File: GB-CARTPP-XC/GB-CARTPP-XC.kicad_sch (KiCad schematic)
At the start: 29 parts

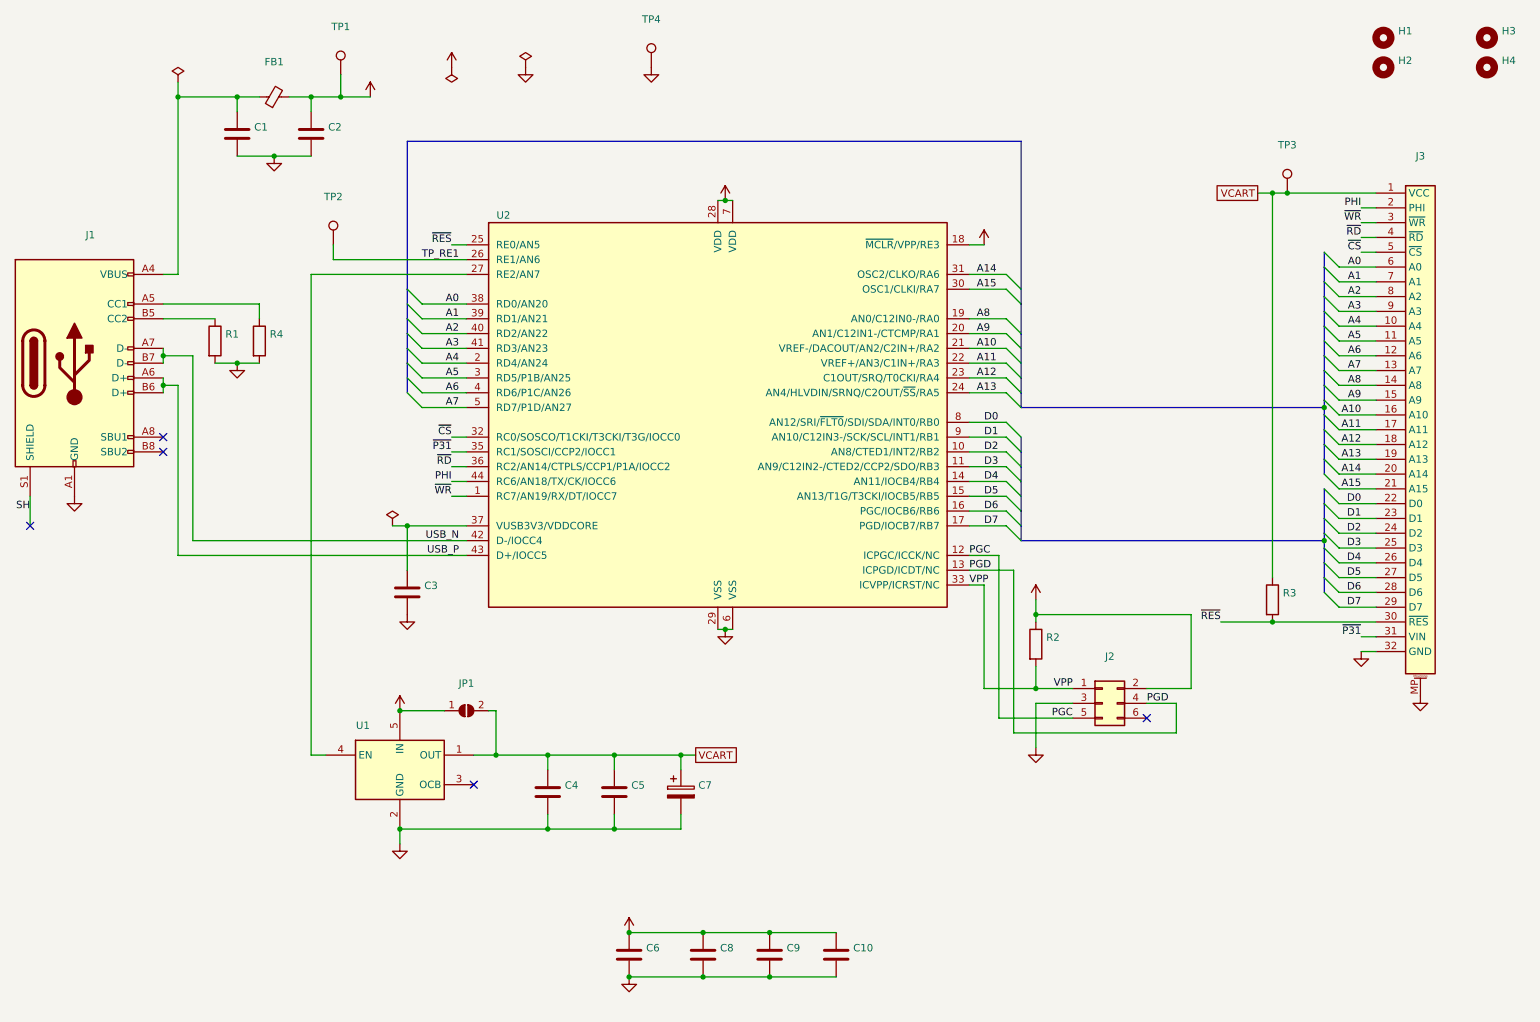
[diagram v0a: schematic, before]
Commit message: Upgrade projects to KiCad 7
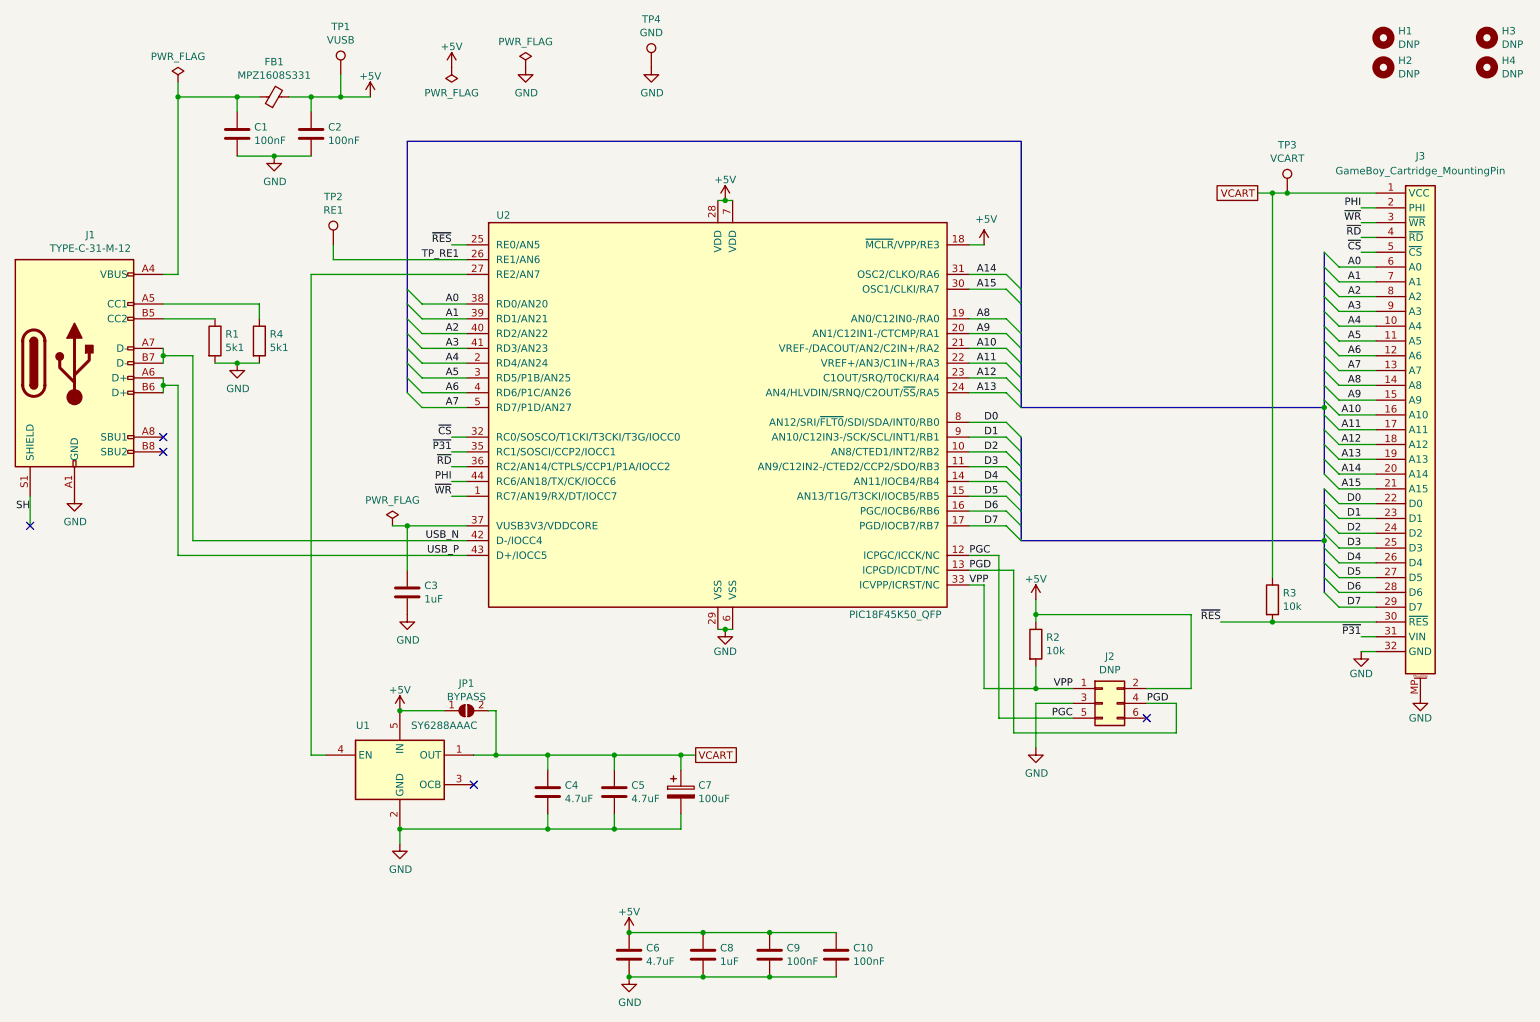
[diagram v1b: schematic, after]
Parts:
- C1, C10, C2, C9: value (none) -> 100nF; footprint (none) -> Capacitor_SMD:C_0603_1608Metric
- C3, C8: value (none) -> 1uF; footprint (none) -> Capacitor_SMD:C_0805_2012Metric
- C4, C5, C6: value (none) -> 4.7uF; footprint (none) -> Capacitor_SMD:C_0805_2012Metric
- C7: value (none) -> 100uF; footprint (none) -> Capacitor_SMD:CP_Elec_6.3x5.8
- FB1: value (none) -> MPZ1608S331; footprint (none) -> Inductor_SMD:L_0603_1608Metric
- H1, H2, H3, H4: value (none) -> DNP; footprint (none) -> MountingHole:MountingHole_3.2mm_M3
- J1: value (none) -> TYPE-C-31-M-12; footprint (none) -> Connector_USB:USB_C_Receptacle_HRO_TYPE-C-31-M-12
- J2: value (none) -> DNP; footprint (none) -> Connector:Tag-Connect_TC2030-IDC-NL_2x03_P1.27mm_Vertical
- J3: value (none) -> GameBoy_Cartridge_MountingPin; footprint (none) -> Gekkio_Connector_PCBEdge:GameBoy_Cartridge_AGS_1x32-1MP_P1.50mm_Socket_Horizontal
- JP1: value (none) -> BYPASS; footprint (none) -> Jumper:SolderJumper-2_P1.3mm_Open_RoundedPad1.0x1.5mm
- R1, R4: value (none) -> 5k1; footprint (none) -> Resistor_SMD:R_0603_1608Metric
- R2, R3: value (none) -> 10k; footprint (none) -> Resistor_SMD:R_0603_1608Metric
- TP1: value (none) -> VUSB; footprint (none) -> TestPoint:TestPoint_THTPad_D2.0mm_Drill1.0mm
- TP2: value (none) -> RE1; footprint (none) -> TestPoint:TestPoint_Pad_D1.0mm
- TP3: value (none) -> VCART; footprint (none) -> TestPoint:TestPoint_THTPad_D2.0mm_Drill1.0mm
- TP4: value (none) -> GND; footprint (none) -> TestPoint:TestPoint_THTPad_D2.0mm_Drill1.0mm
- U1: value (none) -> SY6288AAAC; footprint (none) -> Package_TO_SOT_SMD:SOT-23-5
- U2: value (none) -> PIC18F45K50_QFP; footprint (none) -> Package_QFP:TQFP-44_10x10mm_P0.8mm
